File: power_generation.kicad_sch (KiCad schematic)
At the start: 35 parts, among them J301 61300211121, J302 61300211121, J303 EMI shield frame, U301 AP64500SP-13, U302 AP64500SP-13

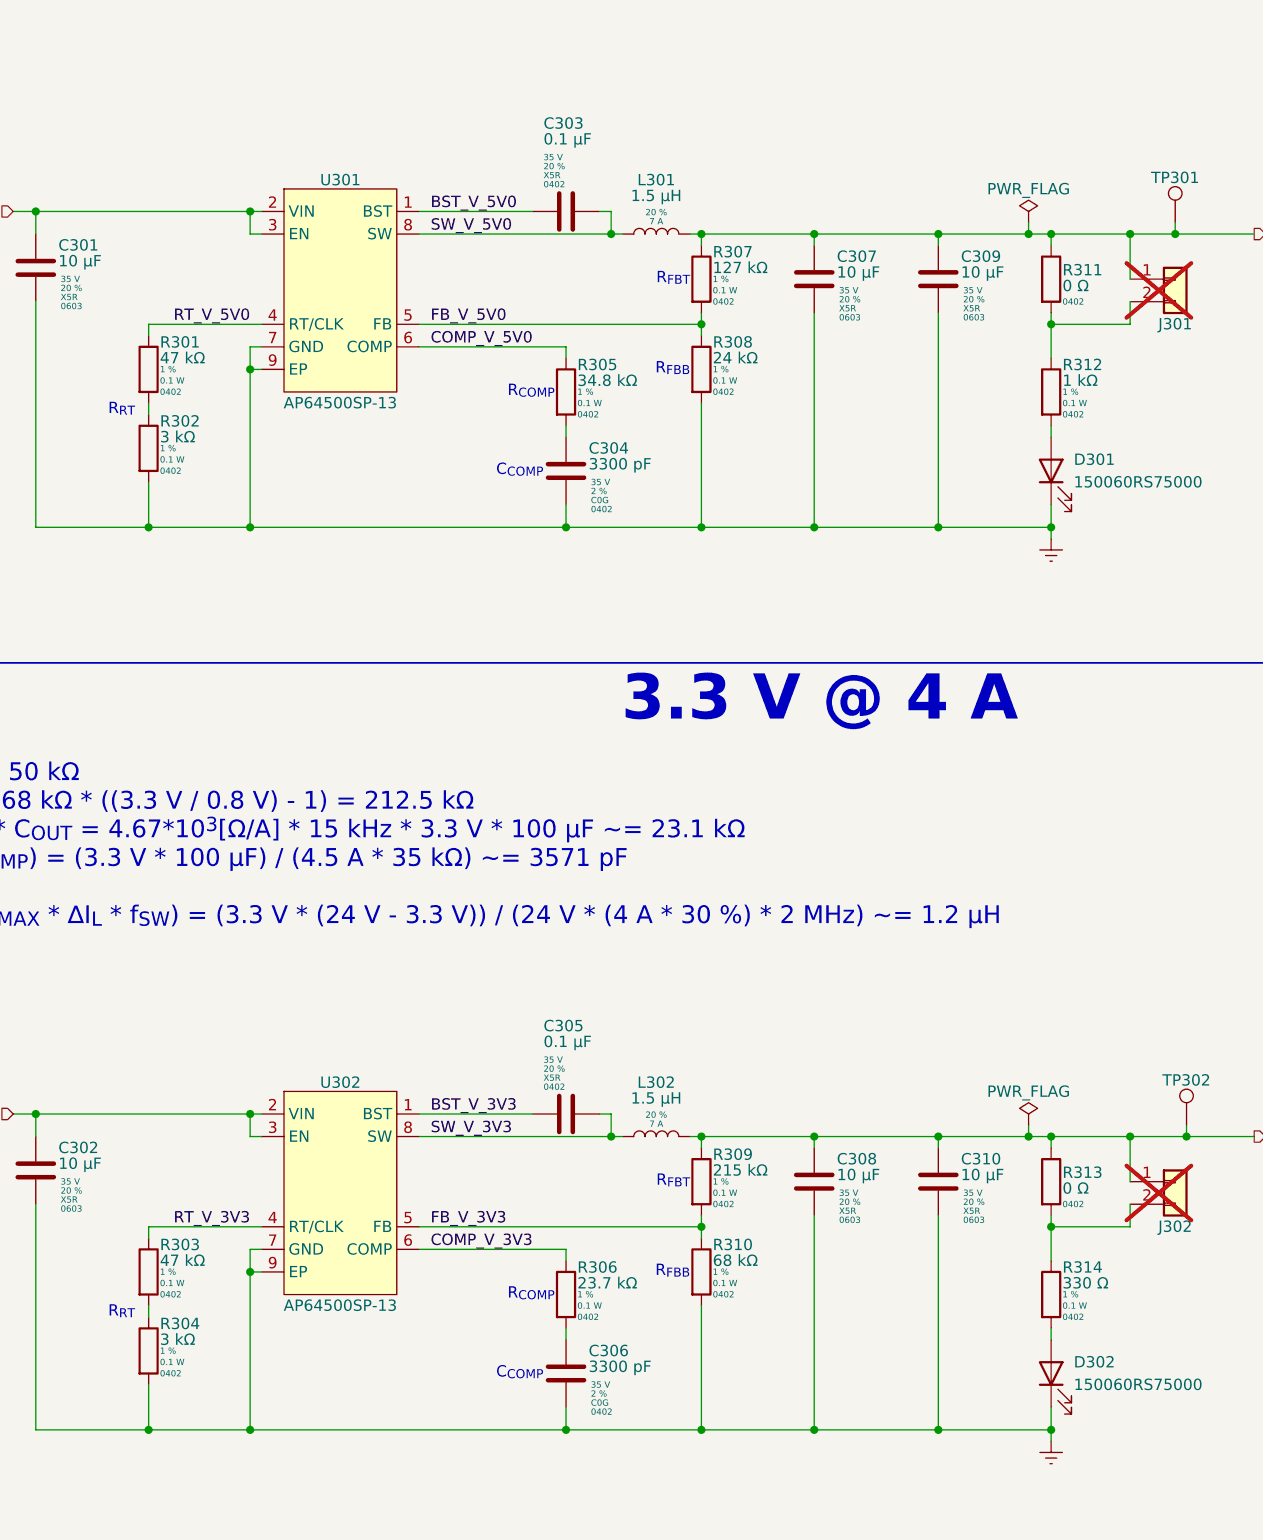
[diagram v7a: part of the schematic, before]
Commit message: 0402 -> 0201 where possible
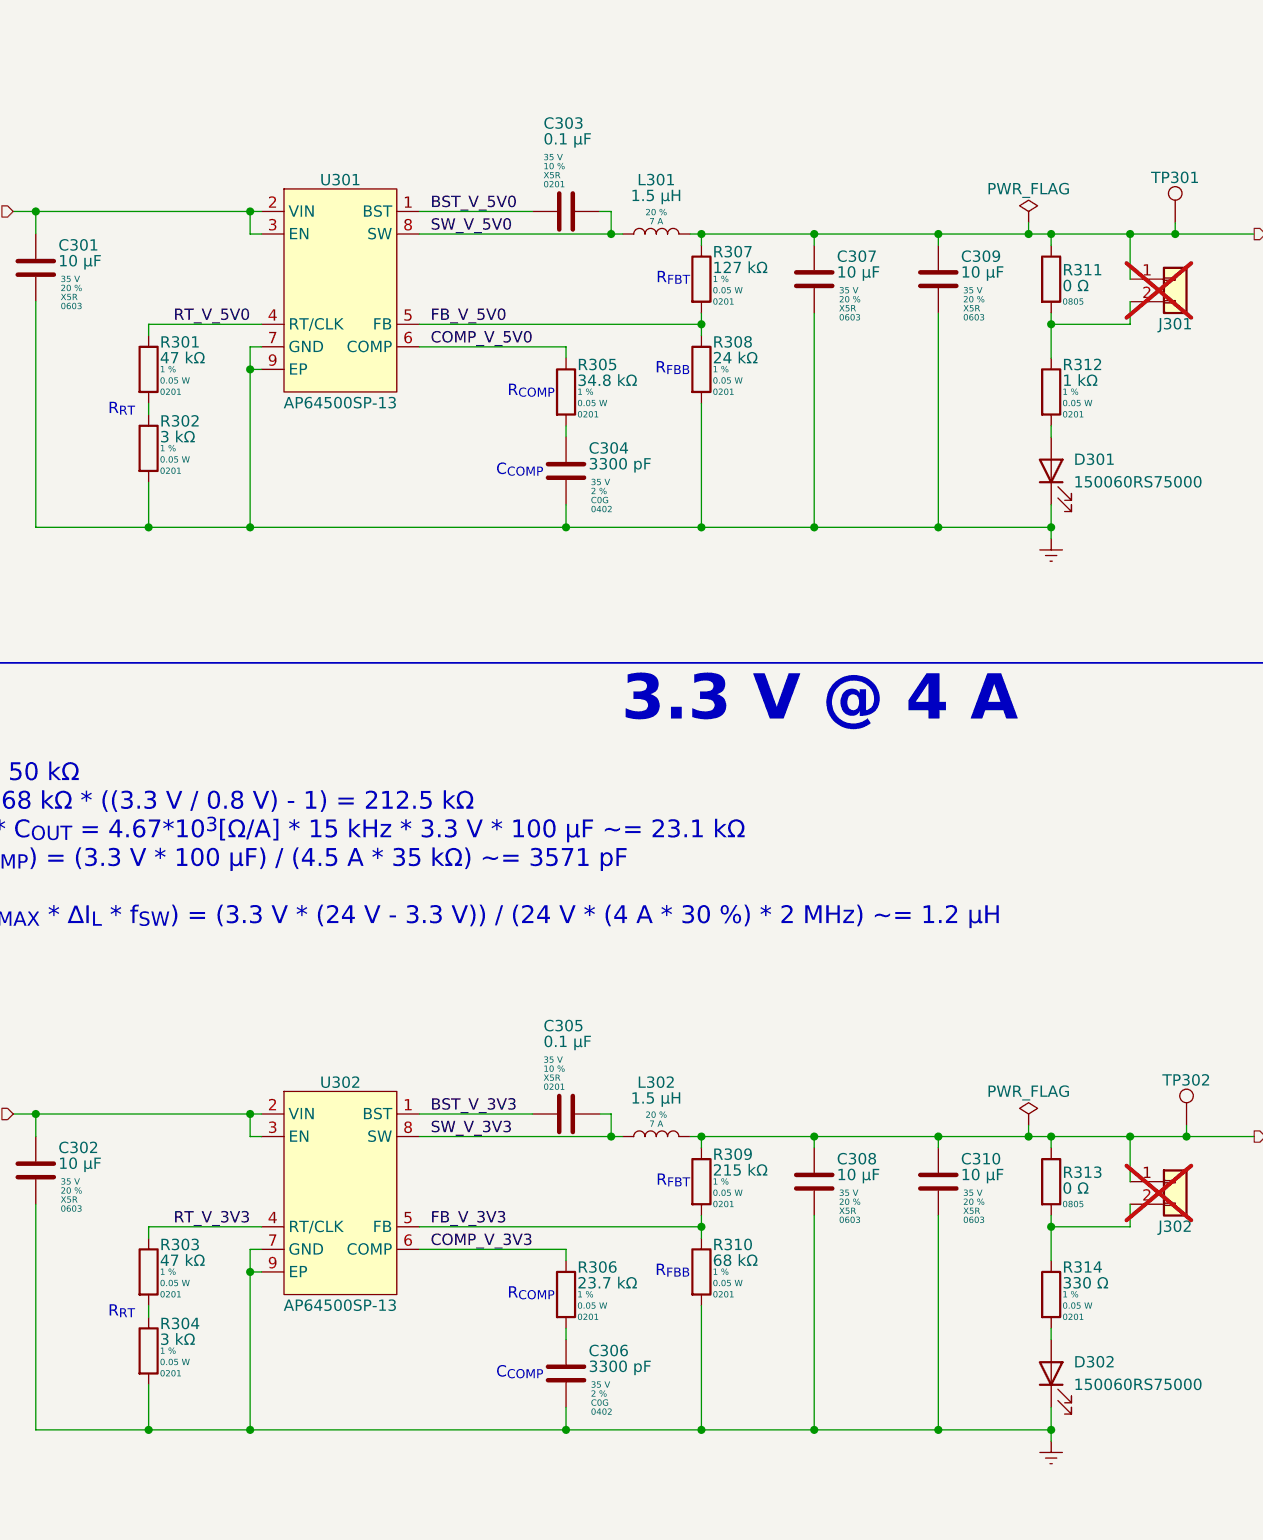
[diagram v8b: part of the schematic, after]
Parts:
- C303, C305: footprint perfect_footprints:C_0402_1005Metric -> Capacitor_SMD:C_0201_0603Metric; Digi-Key Part Number 490-10700-1-ND -> 490-10430-1-ND; MPN GRM155R71H104KE14D -> GRM033R6YA104KE14D; Size 0402 -> 0201; Tolerance 20 % -> 10 %
- R301, R303: footprint perfect_footprints:R_0402_1005Metric -> Resistor_SMD:R_0201_0603Metric; Digi-Key Part Number P47.0KLCT-ND -> P123032CT-ND; MPN ERJ-2RKF4702X -> ERJ-1GNF4702C; Power rating 0.1 W -> 0.05 W; Size 0402 -> 0201
- R302, R304: footprint perfect_footprints:R_0402_1005Metric -> Resistor_SMD:R_0201_0603Metric; Digi-Key Part Number 738-RNCF0402DTE3K00CT-ND -> P122912CT-ND; MPN RNCF0402DTE3K00 -> ERJ-1GNF3001C; Power rating 0.1 W -> 0.05 W; Size 0402 -> 0201
- R305: footprint perfect_footprints:R_0402_1005Metric -> Resistor_SMD:R_0201_0603Metric; Digi-Key Part Number P34.8KLCT-ND -> P122952CT-ND; MPN ERJ-2RKF3482X -> ERJ-1GNF3482C; Power rating 0.1 W -> 0.05 W; Size 0402 -> 0201
- R306: footprint perfect_footprints:R_0402_1005Metric -> Resistor_SMD:R_0201_0603Metric; Digi-Key Part Number P23.7KLCT-ND -> P122852CT-ND; MPN ERJ-2RKF2372X -> ERJ-1GNF2372C; Power rating 0.1 W -> 0.05 W; Size 0402 -> 0201
- R307: footprint perfect_footprints:R_0402_1005Metric -> Resistor_SMD:R_0201_0603Metric; Digi-Key Part Number P127KLCT-ND -> P122707CT-ND; MPN ERJ-2RKF1273X -> ERJ-1GNF1273C; Power rating 0.1 W -> 0.05 W; Size 0402 -> 0201
- R308: footprint perfect_footprints:R_0402_1005Metric -> Resistor_SMD:R_0201_0603Metric; Digi-Key Part Number 732-560112110178CT-ND -> P122858CT-ND; MPN 560112110178 -> ERJ-1GNF2402C; Manufacturer Würth Elektronik -> Panasonic Electronic Components; Power rating 0.1 W -> 0.05 W; Size 0402 -> 0201
- R309: footprint perfect_footprints:R_0402_1005Metric -> Resistor_SMD:R_0201_0603Metric; Digi-Key Part Number P215KLCT-ND -> P122828CT-ND; MPN ERJ-2RKF2153X -> ERJ-1GNF2153C; Power rating 0.1 W -> 0.05 W; Size 0402 -> 0201
- R310: footprint perfect_footprints:R_0402_1005Metric -> Resistor_SMD:R_0201_0603Metric; Digi-Key Part Number 732-560112110035CT-ND -> P123126CT-ND; MPN 560112110035 -> ERJ-1GNF6802C; Manufacturer Würth Elektronik -> Panasonic Electronic Components; Power rating 0.1 W -> 0.05 W; Size 0402 -> 0201
- R311, R313: footprint perfect_footprints:R_0402_1005Metric -> Resistor_SMD:R_0805_2012Metric; Digi-Key Part Number P0.0JCT-ND -> P0.0ACT-ND; MPN ERJ-2GE0R00X -> ERJ-6GEY0R00V; Size 0402 -> 0805
- R312: footprint perfect_footprints:R_0402_1005Metric -> Resistor_SMD:R_0201_0603Metric; Digi-Key Part Number P1.00KLCT-ND -> 10-ERJ-U01F1001CCT-ND; MPN ERJ-2RKF1001X -> ERJ-U01F1001C; Power rating 0.1 W -> 0.05 W; Size 0402 -> 0201
- R314: footprint perfect_footprints:R_0402_1005Metric -> Resistor_SMD:R_0201_0603Metric; Digi-Key Part Number 732-560112110231CT-ND -> P122936CT-ND; MPN 560112110231 -> ERJ-1GNF3300C; Manufacturer Würth Elektronik -> Panasonic Electronic Components; Power rating 0.1 W -> 0.05 W; Size 0402 -> 0201
